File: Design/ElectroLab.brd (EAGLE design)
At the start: 175 x 100 mm, 229 parts, among them IC11 PAM8403, IC13 74HC08DD, IC14 74HC04DD, IC15 74HC32S14-13, IC3 LM324DTD, IC4 LM324DTD, IC6 MC74HC112ADR2G, IC7 MC74HC112ADR2G, IC8 TLC555CDR, IC9 TP4056, J13 AUDIO_JACK_MONO_3.5LCSC, P1 SLIDE_POT_20MM, T1 MMBT2222A, T2 T_NPNMMBT2222A-1P_CHANGJ_SOT2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, T3 T_NPNMMBT2222A-1P_CHANGJ_SOT2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, T4 T_PNPMMBT5401_CHANGJ_SOT23-BEC, T5 T_PNPMMBT5401_CHANGJ_SOT23-BEC, U1 ADXL335, U2 GAS_SENSOR, U3 AMS1117-3.3VSMD, X8 USB-C-POWER

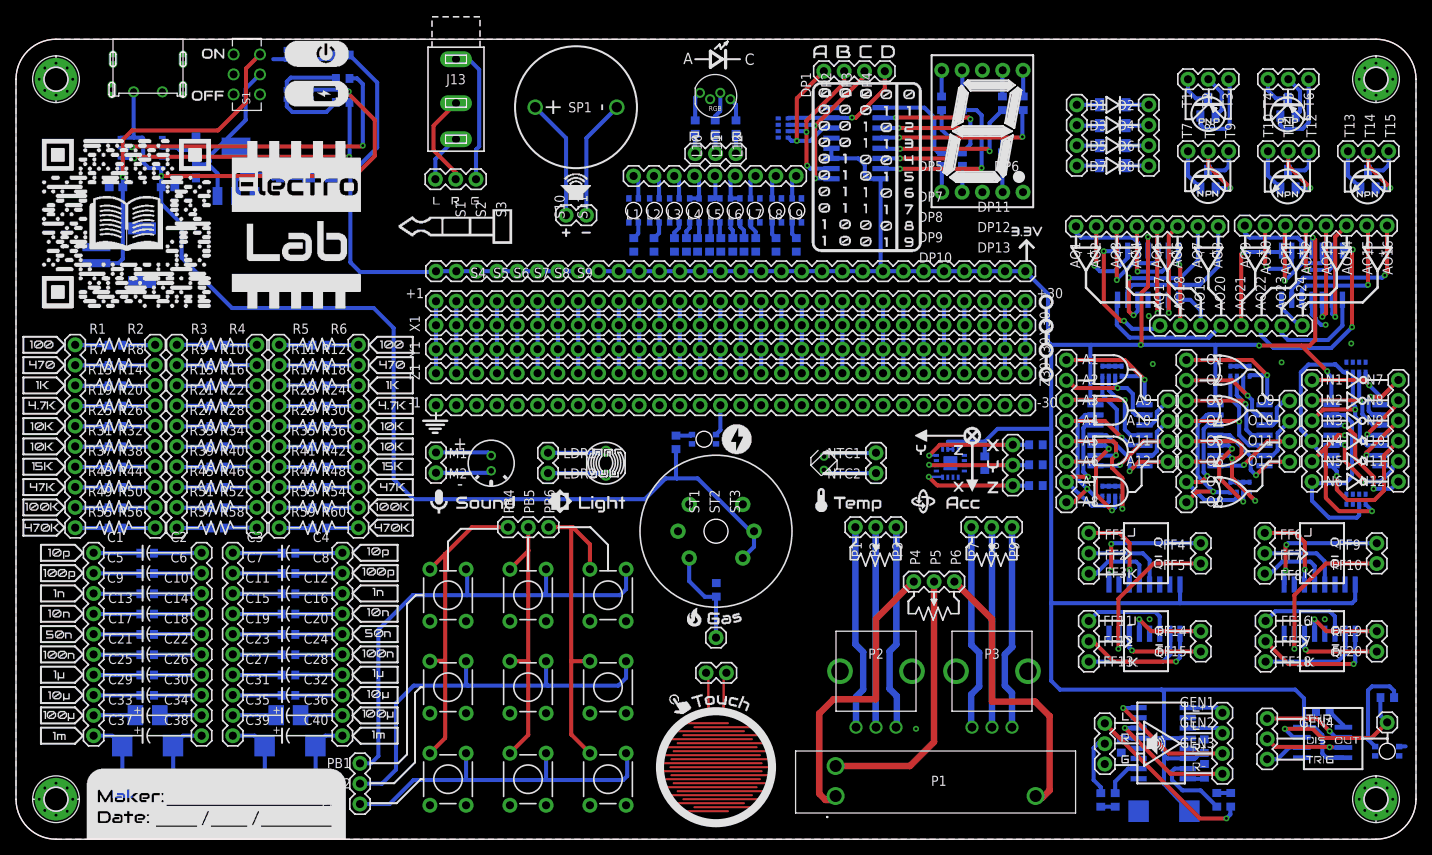
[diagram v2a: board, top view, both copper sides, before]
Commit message: Replaced Jack connector MQ-2 sensor power through main switch
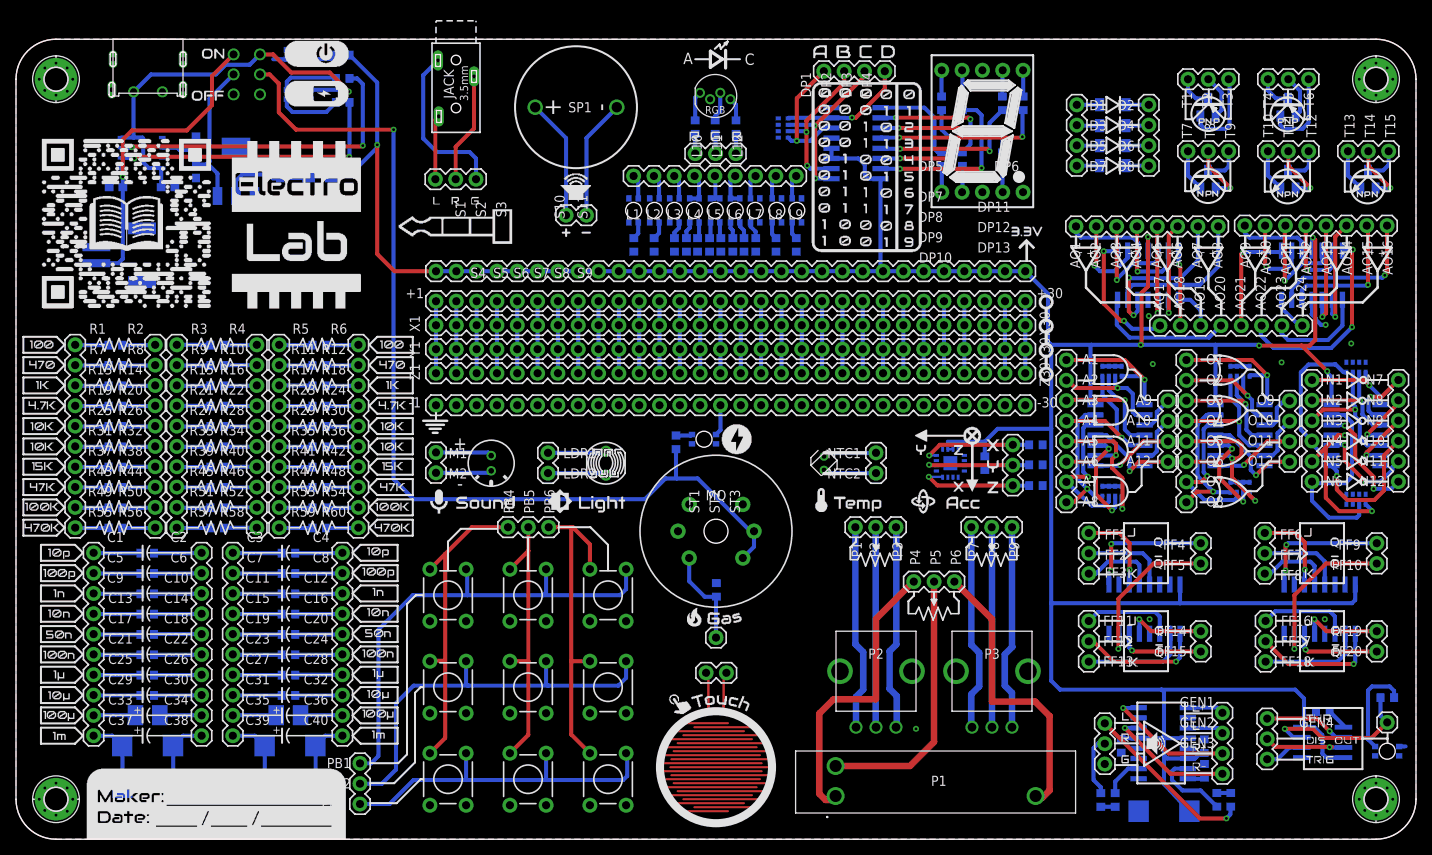
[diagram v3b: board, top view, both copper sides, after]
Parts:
- removed J13: AUDIO_JACK_MONO_3.5LCSC, SpaceDIY_connectors:PJ316
- added JACK: AUDIO_JACK_MONO_3.5_3P, SpaceDIY_connectors:HC-PJ-320A-3P-D
- flipped S1 to the bottom
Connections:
- removed net VIN: C37.1, IC9.4, IC9.8, LED1.2, LED1.3, R38.2, U2.A1, U2.HA, X8.VBUS
- new net 5V: R38.2, S1.2, U2.A1, U2.HA
- new net V_USB: C37.1, IC9.4, IC9.8, LED1.2, LED1.3, S1.1, X8.VBUS
- net N$102: now also JACK.2; no longer J13.2
- net N$116: now also JACK.1; no longer J13.1
- net N$264: now also JACK.3; no longer J13.3
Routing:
- net VIN: track 176.3 -> 0.00 mm, vias 2 -> 0
- net 5V: track 0.00 -> 122.9 mm, vias 0 -> 1
- net V_USB: track 0.00 -> 53.5 mm, vias 0 -> 1
- net VBAT: track 43.7 -> 40.0 mm
- net N$116: track 17.3 -> 20.8 mm
- net N$102: track 11.8 -> 13.8 mm
- net N$264: track 6.13 -> 8.03 mm
- net N$109: track 19.9 -> 18.5 mm
- net VCC: vias 5 -> 6
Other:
- board text added: "3.5mm"
- board text added: "MQ"

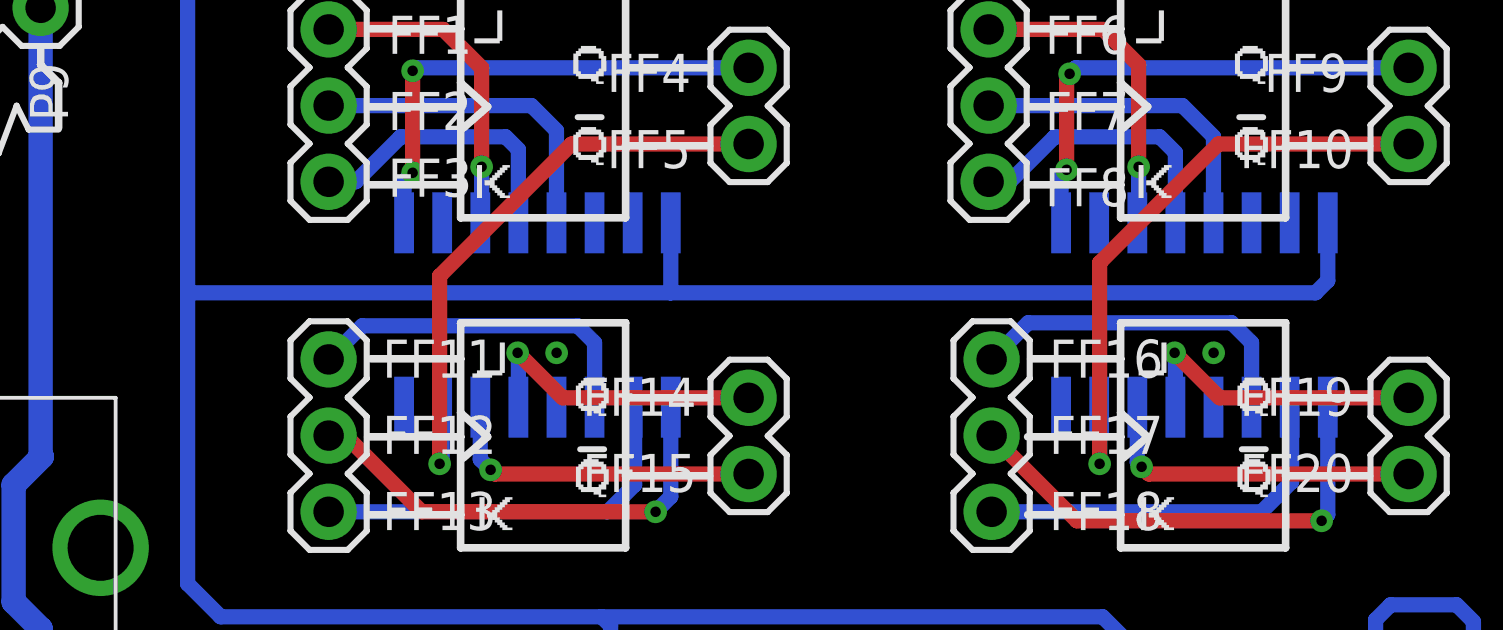
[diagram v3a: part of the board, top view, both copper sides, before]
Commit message: Set & reset connected to VCC (3.3V) instead of GND
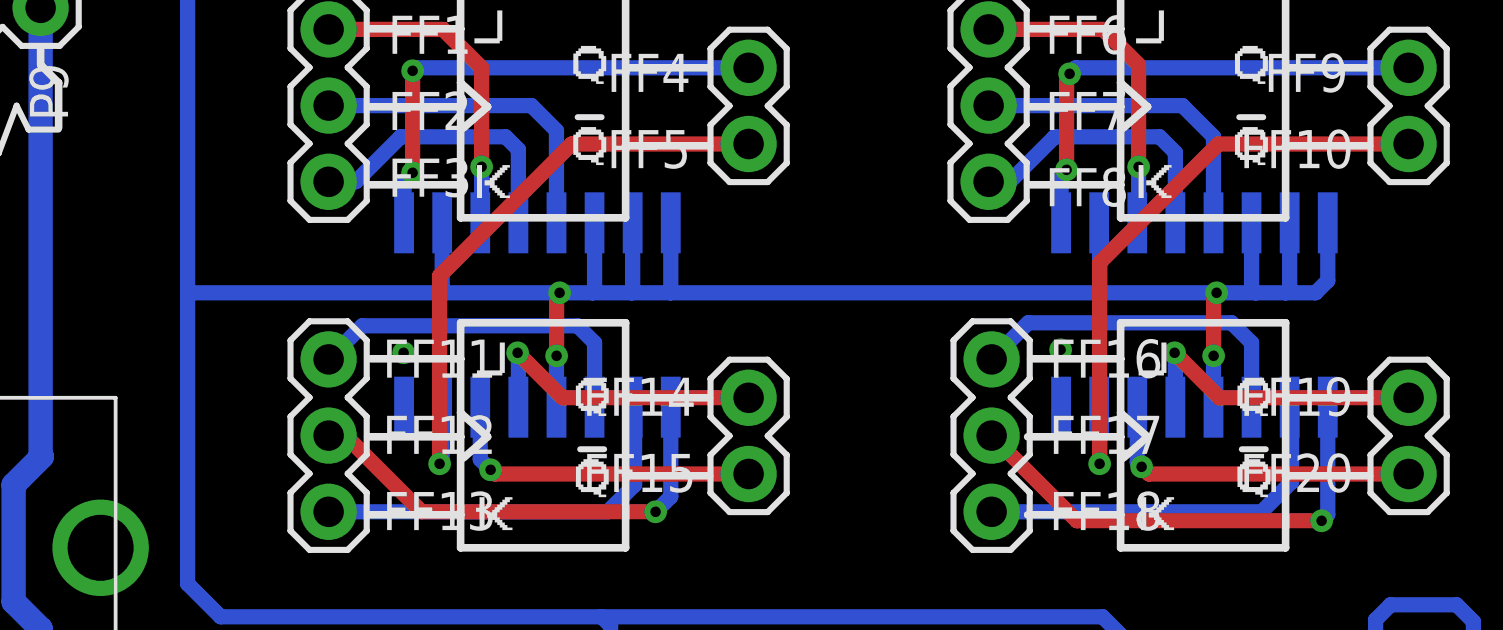
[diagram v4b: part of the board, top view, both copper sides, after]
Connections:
- net GND: no longer IC6.10, IC6.14, IC6.15, IC6.4, IC7.10, IC7.14, IC7.15, IC7.4
- net VCC: now also IC6.10, IC6.14, IC6.15, IC6.4, IC7.10, IC7.14, IC7.15, IC7.4
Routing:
- net VCC: track 412.6 -> 434.5 mm, vias 6 -> 10
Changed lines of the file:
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@@
 <setting verticaltext="up"/>
 </settings>
-<grid distance="0.5" unitdist="mm" unit="mm" style="lines" multiple="1" display="yes" altdistance="0.025" altunitdist="inch" altunit="inch"/>
+<grid distance="0.1" unitdist="mm" unit="mm" style="lines" multiple="1" display="yes" altdistance="0.025" altunitdist="inch" altunit="inch"/>
 <layers>
 <layer number="1" name="Top" color="4" fill="1" visible="yes" active="yes"/>
@@
 <contactref element="IC6" pad="8"/>
 <contactref element="IC7" pad="8"/>
-<contactref element="IC6" pad="4"/>
-<contactref element="IC6" pad="15"/>
-<contactref element="IC6" pad="10"/>
-<contactref element="IC6" pad="14"/>
-<contactref element="IC7" pad="4"/>
-<contactref element="IC7" pad="15"/>
-<contactref element="IC7" pad="10"/>
-<contactref element="IC7" pad="14"/>
 <contactref element="IC11" pad="9"/>
 <contactref element="IC11" pad="11"/>
@@
 <via x="3.6" y="93.6" extent="1-16" drill="0.35"/>
 <via x="112.5" y="13.8" extent="1-16" drill="0.35"/>
-<via x="141.7" y="27.5" extent="1-16" drill="0.35"/>
-<via x="163.6" y="27.5" extent="1-16" drill="0.35"/>
 <wire x1="170" y1="95" x2="170" y2="93.8372" width="0.508" layer="1"/>
 <via x="166.9016" y="61.9655" extent="1-16" drill="0.35"/>
@@
 <wire x1="87.5" y1="50.585" x2="88.06" y2="51.145" width="0.508" layer="16"/>
 <wire x1="88.06" y1="51.145" x2="88.06" y2="54.25" width="0.508" layer="16"/>
+<via x="158.5" y="27.6" extent="1-16" drill="0.35"/>
+<via x="136.6" y="27.5" extent="1-16" drill="0.35"/>
 <wire x1="172.9" y1="11.585" x2="170" y2="5" width="0" layer="19" extent="16-16"/>
 <wire x1="6.4" y1="93.5" x2="5" y2="93" width="0" layer="19" extent="1-1"/>
@@
 <wire x1="106.545" y1="82.555" x2="108.0734" y2="82.555" width="0.508" layer="16"/>
 <wire x1="105.305" y1="85.095" x2="106.1" y2="84.3" width="0.508" layer="16"/>
-<wire x1="129.4" y1="29.5" x2="145.5" y2="29.5" width="0.508" layer="16"/>
-<wire x1="145.5" y1="29.5" x2="167" y2="29.5" width="0.508" layer="16"/>
+<wire x1="129.4" y1="29.5" x2="137.7" y2="29.5" width="0.508" layer="16"/>
+<wire x1="137.7" y1="29.5" x2="141.8" y2="29.5" width="0.508" layer="16"/>
+<wire x1="141.8" y1="29.5" x2="142.9" y2="29.5" width="0.508" layer="16"/>
+<wire x1="142.9" y1="29.5" x2="144.2" y2="29.5" width="0.508" layer="16"/>
+<wire x1="144.2" y1="29.5" x2="145.5" y2="29.5" width="0.508" layer="16"/>
+<wire x1="145.5" y1="29.5" x2="159.8" y2="29.5" width="0.508" layer="16"/>
+<wire x1="159.8" y1="29.5" x2="163.7" y2="29.5" width="0.508" layer="16"/>
+<wire x1="163.7" y1="29.5" x2="165" y2="29.5" width="0.508" layer="16"/>
+<wire x1="165" y1="29.5" x2="166" y2="29.5" width="0.508" layer="16"/>
+<wire x1="166" y1="29.5" x2="167" y2="29.5" width="0.508" layer="16"/>
 <wire x1="167.405" y1="29.905" x2="167.405" y2="31.8334" width="0.508" layer="16"/>
 <wire x1="167" y1="29.5" x2="167.405" y2="29.905" width="0.508" layer="16"/>
@@
 <via x="45.15" y="86.8" extent="1-16" drill="0.35"/>
 <wire x1="47.3" y1="71" x2="45.15" y2="73.15" width="0.508" layer="1"/>
+<contactref element="IC6" pad="4"/>
+<contactref element="IC6" pad="15"/>
+<contactref element="IC6" pad="10"/>
+<contactref element="IC6" pad="14"/>
+<contactref element="IC7" pad="4"/>
+<contactref element="IC7" pad="15"/>
+<contactref element="IC7" pad="10"/>
+<contactref element="IC7" pad="14"/>
+<wire x1="164.865" y1="31.8334" x2="164.865" y2="29.635" width="0.508" layer="16"/>
+<wire x1="164.865" y1="29.635" x2="165" y2="29.5" width="0.508" layer="16"/>
+<wire x1="166.135" y1="31.8334" x2="166.135" y2="29.635" width="0.508" layer="16"/>
+<wire x1="166.135" y1="29.635" x2="166" y2="29.5" width="0.508" layer="16"/>
+<wire x1="163.595" y1="25.6866" x2="163.595" y2="27.395" width="0.508" layer="16"/>
+<wire x1="163.595" y1="27.395" x2="163.6" y2="27.4" width="0.508" layer="16"/>
+<via x="163.6" y="27.4" extent="1-16" drill="0.35"/>
+<wire x1="163.6" y1="27.4" x2="163.6" y2="29.4" width="0.508" layer="1"/>
+<wire x1="163.6" y1="29.4" x2="163.7" y2="29.5" width="0.508" layer="1"/>
+<via x="163.7" y="29.5" extent="1-16" drill="0.35"/>
+<wire x1="159.785" y1="31.8334" x2="159.8" y2="31.8184" width="0.508" layer="16"/>
+<wire x1="159.8" y1="31.8184" x2="159.8" y2="29.5" width="0.508" layer="16"/>
+<wire x1="144.235" y1="31.8334" x2="144.235" y2="29.535" width="0.508" layer="16"/>
+<wire x1="144.235" y1="29.535" x2="144.2" y2="29.5" width="0.508" layer="16"/>
+<wire x1="142.965" y1="31.8334" x2="142.965" y2="29.565" width="0.508" layer="16"/>
+<wire x1="142.965" y1="29.565" x2="142.9" y2="29.5" width="0.508" layer="16"/>
+<wire x1="141.695" y1="25.6866" x2="141.695" y2="27.395" width="0.508" layer="16"/>
+<wire x1="141.695" y1="27.395" x2="141.7" y2="27.4" width="0.508" layer="16"/>
+<via x="141.7" y="27.4" extent="1-16" drill="0.35"/>
+<wire x1="141.7" y1="27.4" x2="141.7" y2="29.4" width="0.508" layer="1"/>
+<wire x1="141.7" y1="29.4" x2="141.8" y2="29.5" width="0.508" layer="1"/>
+<via x="141.8" y="29.5" extent="1-16" drill="0.35"/>
+<wire x1="137.885" y1="31.8334" x2="137.885" y2="29.685" width="0.508" layer="16"/>
+<wire x1="137.885" y1="29.685" x2="137.7" y2="29.5" width="0.508" layer="16"/>
 <wire x1="121.08" y1="71" x2="123.62" y2="71" width="0" layer="19" extent="1-1"/>
 <wire x1="118.54" y1="71" x2="121.08" y2="71" width="0" layer="19" extent="1-1"/>

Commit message: Added design files
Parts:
- S1: value (none) -> DPDT_JS202011CQN; device bt_electromech:DPDT_JS202011CQN -> SpaceDIY_electromechanical:DPDT_JS202011CQN
- flipped S1 to the top, turned to 90 degrees
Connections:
- net VBAT: now also S1.6; no longer S1.4
- net V_USB: now also S1.3; no longer S1.1
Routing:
- net VBAT: track 40.0 -> 41.1 mm
- net N$109: vias 0 -> 1
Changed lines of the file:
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@@
 <attribute name="VALUE" x="16.416" y="10.725" size="1.016" layer="28" rot="MR0" align="center"/>
 </element>
-<element name="S1" library="bt_electromech" package="DPDT_JS202011CQN" value="" x="28.85" y="95.6" smashed="yes" rot="MR270">
-<attribute name="NAME" x="28.9262" y="92.6738" size="1.016" layer="26" rot="MR270" align="center"/>
-<attribute name="VALUE" x="26.056" y="99.283" size="1.27" layer="28" rot="MR270"/>
+<element name="S1" library="SpaceDIY_electromechanical" package="DPDT_JS202011CQN" value="DPDT_JS202011CQN" x="28.85" y="95.6" smashed="yes" rot="R90">
+<attribute name="LCSC" value="C189615" x="28.85" y="95.6" size="1.778" layer="27" rot="R90" display="off"/>
+<attribute name="NAME" x="28.8738" y="92.5262" size="1.016" layer="25" rot="R180" align="center"/>
+<attribute name="VALUE" x="26.056" y="91.917" size="1.27" layer="27" rot="R90"/>
 </element>
 <element name="R31" library="SpaceDIY_passive_components" package="0603" value="470" x="40.85" y="98.02" smashed="yes" rot="MR0">
@@
 <contactref element="IC9" pad="5"/>
 <contactref element="C28" pad="1"/>
-<contactref element="S1" pad="4"/>
 <contactref element="J1" pad="1"/>
 <wire x1="13.35" y1="81.5" x2="13.35" y2="82.8" width="0.508" layer="16"/>
@@
 <wire x1="13.35" y1="87.45" x2="13.35" y2="82.8" width="0.508" layer="1"/>
 <via x="13.35" y="82.8" extent="1-16" drill="0.35"/>
-<wire x1="21.35" y1="88.6" x2="24.5" y2="91.75" width="0.508" layer="1"/>
-<wire x1="24.5" y1="95.4" x2="27.2" y2="98.1" width="0.508" layer="1"/>
-<wire x1="24.5" y1="91.75" x2="24.5" y2="95.4" width="0.508" layer="1"/>
+<wire x1="21.35" y1="88.6" x2="22.8" y2="90.05" width="0.508" layer="1"/>
+<wire x1="22.8" y1="90.05" x2="22.8" y2="95.6" width="0.508" layer="1"/>
+<contactref element="S1" pad="6"/>
+<wire x1="22.8" y1="95.6" x2="25.3" y2="98.1" width="0.508" layer="1"/>
+<wire x1="25.3" y1="98.1" x2="27.2" y2="98.1" width="0.508" layer="1"/>
 </signal>
 <signal name="N$104">
@@
 <wire x1="82.5" y1="45.2" x2="82.6" y2="45.1" width="0.508" layer="16"/>
 <contactref element="S1" pad="2"/>
-<wire x1="30.501" y1="95.6" x2="31.7" y2="95.6" width="0.508" layer="1"/>
 <wire x1="32.85" y1="94.45" x2="31.7" y2="95.6" width="0.508" layer="1"/>
 <via x="47.2" y="88.7" extent="1-16" drill="0.35"/>
@@
 <wire x1="47.2" y1="45" x2="47.2" y2="88.7" width="0.508" layer="16"/>
 <wire x1="35" y1="88.7" x2="32.85" y2="90.85" width="0.508" layer="1"/>
+<wire x1="31.7" y1="95.6" x2="30.501" y2="95.6" width="0.508" layer="1"/>
 </signal>
 <signal name="VOUT">
@@
 <wire x1="25.1886" y1="80.4012" x2="25.1886" y2="83.2114" width="0.508" layer="16"/>
 <wire x1="25.1886" y1="83.2114" x2="23.95" y2="84.45" width="0.508" layer="16"/>
-<wire x1="24.2" y1="92.601" x2="27.199" y2="95.6" width="0.508" layer="16"/>
+<wire x1="24.2" y1="92.601" x2="27.199" y2="95.6" width="0.508" layer="1"/>
 <wire x1="24.2" y1="84.7" x2="24.2" y2="92.601" width="0.508" layer="16"/>
+<via x="24.2" y="92.601" extent="1-16" drill="0.35"/>
 </signal>
 <signal name="N$102">
@@
 <contactref element="LED1" pad="3"/>
 <contactref element="LED1" pad="2"/>
-<contactref element="S1" pad="1"/>
 <wire x1="18.15" y1="81.5" x2="18.15" y2="83.765" width="0.508" layer="16"/>
 <wire x1="18.15" y1="83.765" x2="18.28" y2="83.895" width="0.508" layer="16"/>
@@
 <wire x1="14.7" y1="93.42" x2="14.7" y2="87.755" width="0.508" layer="16"/>
 <wire x1="14.7" y1="87.755" x2="14.75" y2="87.705" width="0.508" layer="16"/>
-<wire x1="30.5" y1="98.1" x2="32.13973125" y2="98.1" width="0.508" layer="1"/>
-<wire x1="32.13973125" y1="98.1" x2="34.40973125" y2="95.83" width="0.508" layer="1"/>
+<wire x1="34.40973125" y1="95.83" x2="32.13973125" y2="98.1" width="0.508" layer="1"/>
 <wire x1="14.7" y1="93.42" x2="16.88" y2="95.6" width="0.508" layer="16"/>
-<wire x1="29.213" y1="96.813" x2="30.5" y2="98.1" width="0.508" layer="16"/>
 <wire x1="26.213" y1="96.813" x2="29.213" y2="96.813" width="0.508" layer="16"/>
 <wire x1="16.88" y1="95.6" x2="25" y2="95.6" width="0.508" layer="16"/>
@@
 <wire x1="39.22" y1="95.83" x2="41.6" y2="93.45" width="0.508" layer="1"/>
 <wire x1="34.40973125" y1="95.83" x2="39.22" y2="95.83" width="0.508" layer="1"/>
+<contactref element="S1" pad="3"/>
+<wire x1="29.213" y1="96.813" x2="30.5" y2="98.1" width="0.508" layer="16"/>
+<wire x1="32.13973125" y1="98.1" x2="30.5" y2="98.1" width="0.508" layer="1"/>
 </signal>
 </signals>
